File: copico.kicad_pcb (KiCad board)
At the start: 2 copper layers, 100 x 96 mm, 33 parts, among them P1 CocoEdgeConnector, P10 Power Bus, P2 5V Data Bus, P3 3.3V Data Bus, P4 5V Address Bus, P5 3.3V Address Bus, U1 74LS133, U2 74LS06, U3 PicoW, U4 TRANSCEIVER-8BIT, U5 TRANSCEIVER-8BIT, U6 TRANSCEIVER-8BIT, U7 SN74LVC4245A, U8 TRANSCEIVER-8BIT

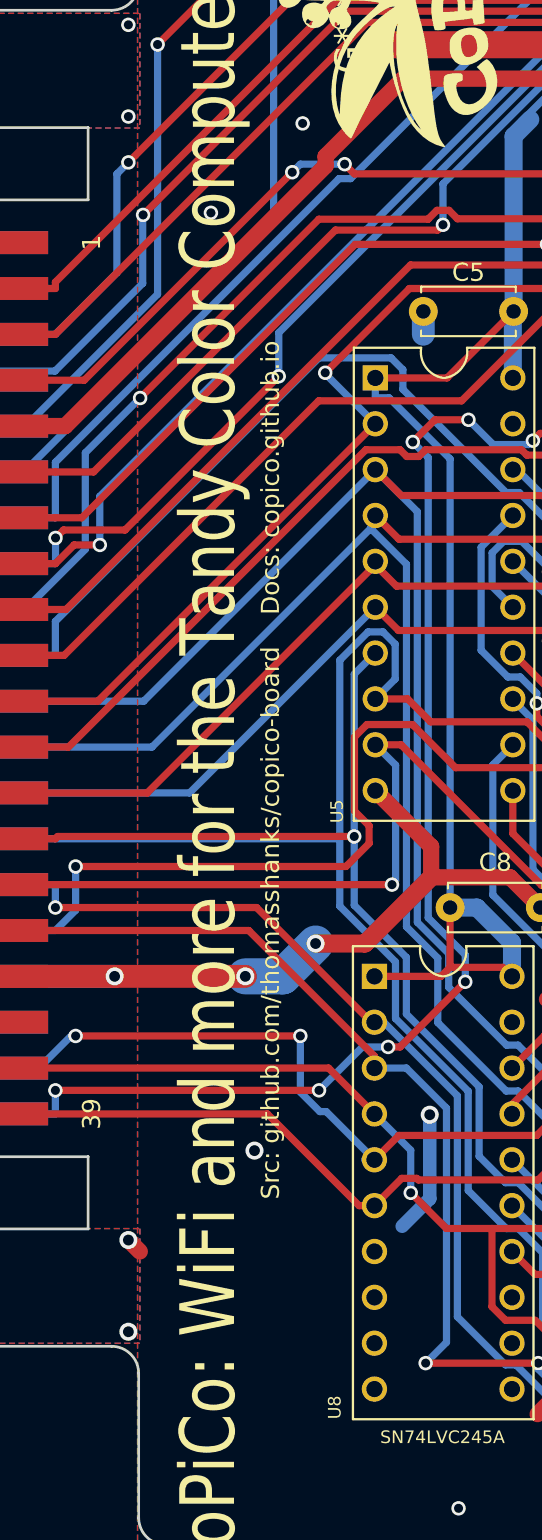
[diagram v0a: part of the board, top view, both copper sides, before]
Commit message: Correct signal naming on schematic & URL on PCB
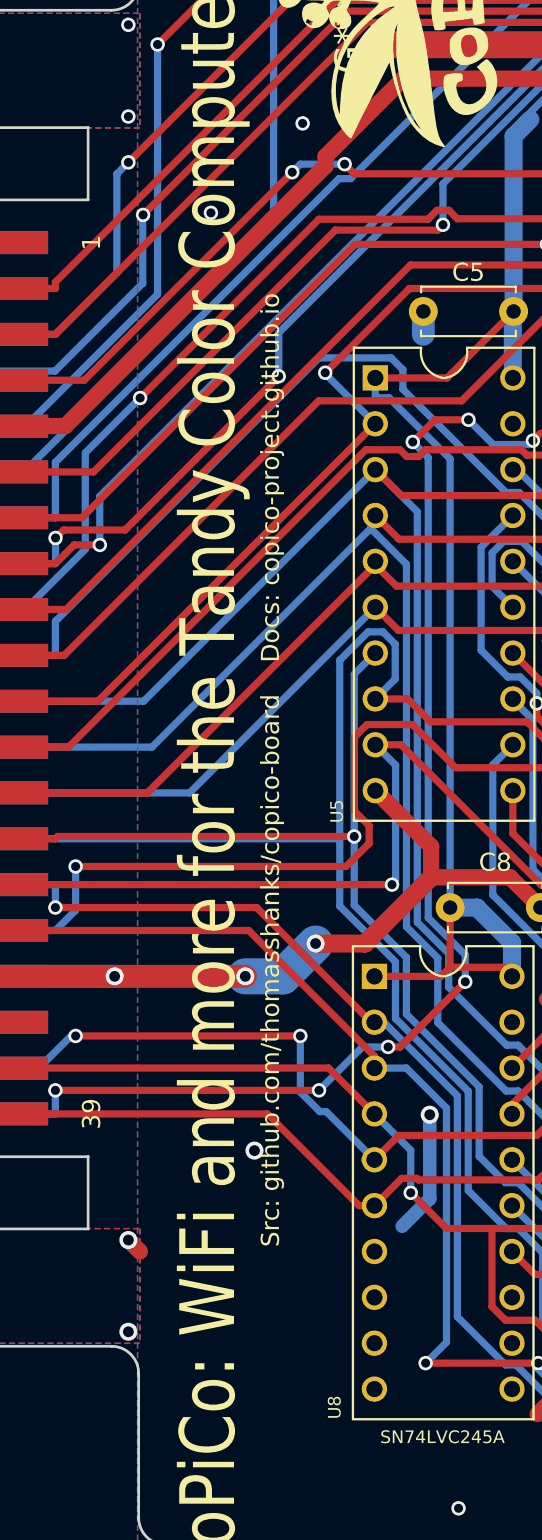
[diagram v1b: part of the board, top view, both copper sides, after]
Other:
- board text added: "Src: github.com/thomasshanks/copico-board Docs: copico-project.github.io"
- board text removed: "Src: github.com/thomasshanks/copico-board Docs: copico.github.io"
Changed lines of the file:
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@@
   (title_block
     (title "CoPiCo: WiFi and more for the Tandy Color Computer")
-    (date "2024-02-07")
-    (rev "0.2.1")
+    (date "2024-02-18")
+    (rev "0.1.22")
     (company "Thomas Shanks (copico@tshanks.org)")
-    (comment 1 "https://github.com/JayesonLS/TandyCircuitsAndLogic/tree/master/CoCoProtoBoard")
-    (comment 2 "Board footprint based on the Public Domain CoCoProtoBoard:")
-    (comment 4 "https://github.com/thomasshanks/copico-board")
+    (comment 1 "found at: github.com/JayesonLS/TandyCircuitsAndLogic/tree/master/CoCoProtoBoard")
+    (comment 2 "Board footprint based on the Public Domain CoCoProtoBoard, which can be")
+    (comment 3 "Released under the MIT License (opensource.org/license/mit)")
+    (comment 4 "GitHub Repo: https://github.com/thomasshanks/copico-board")
   )
   (layers
@@
     (effects (font (size 1.0668 1.0668) (thickness 0.1778)) (justify left bottom mirror))
   )
-  (gr_text "Src: github.com/thomasshanks/copico-board    Docs: copico.github.io" (at 110.744 109.22 90) (layer "F.SilkS")
+  (gr_text "Src: github.com/thomasshanks/copico-board    Docs: copico-project.github.io" (at 110.744 109.22 90) (layer "F.SilkS")
     (effects (font (size 1 1) (thickness 0.15)))
   )

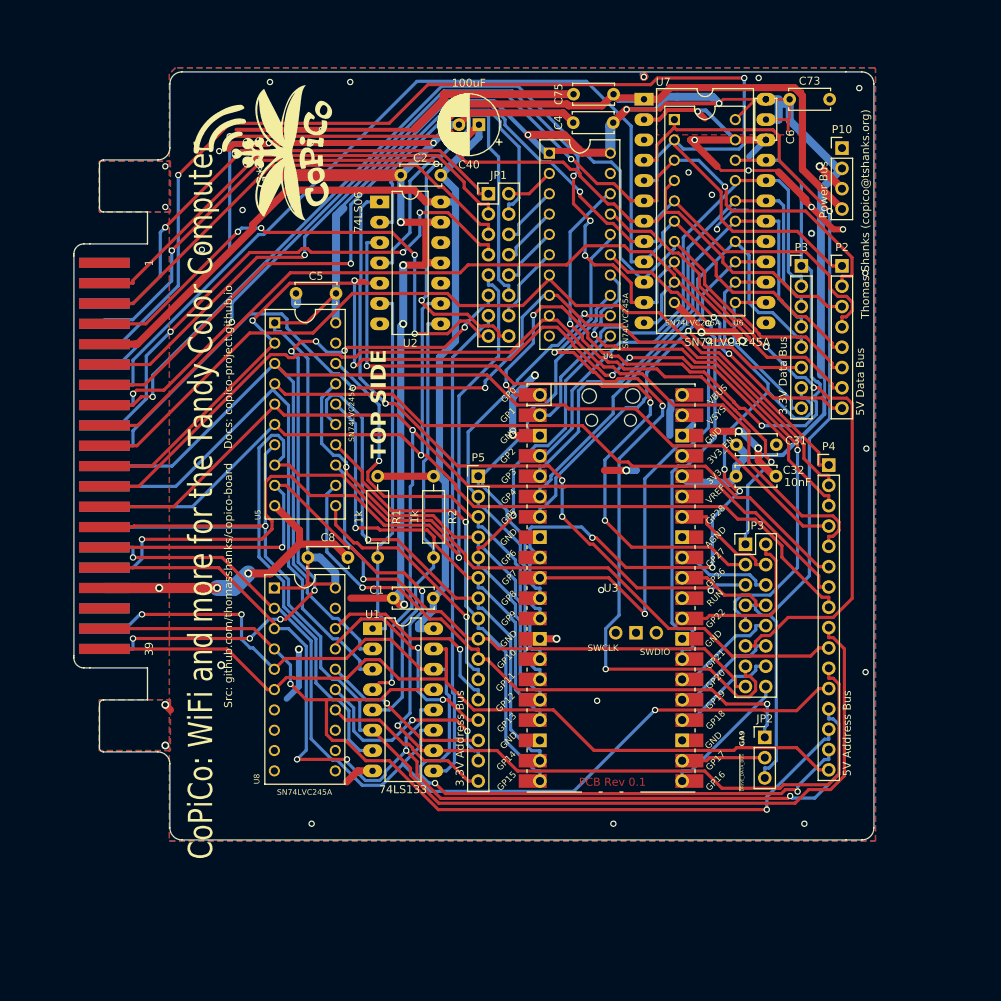
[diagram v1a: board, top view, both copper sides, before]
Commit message: Update silkscreen with component values
I accidentally left the component value silkscreening off the first run of the
board. Add these back, as well as adding some labels to the jumpers and such.

Update PCB Rev in solder mask to 0.1a, but leave the copper layer PCB Rev at
0.1 since that layer has not changed.
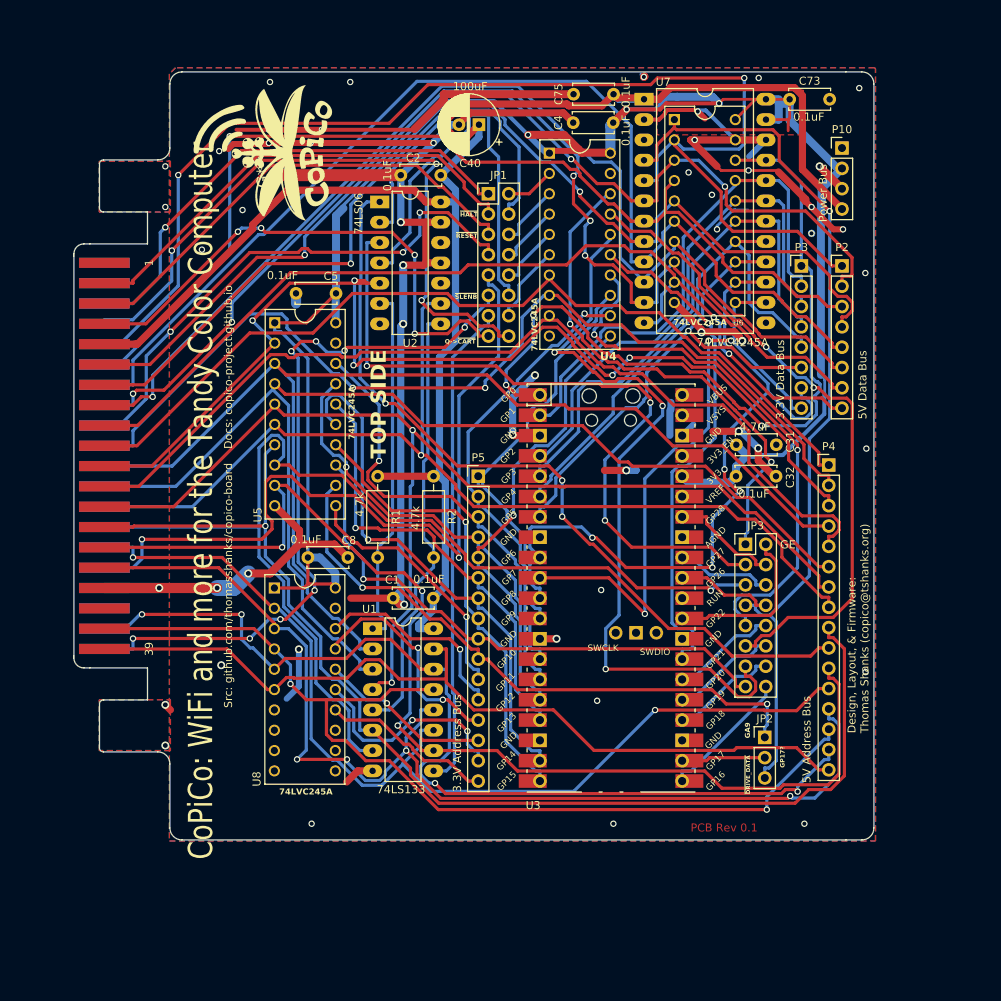
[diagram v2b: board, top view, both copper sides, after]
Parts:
- removed C6: 1uF, 00_Custom:C_Disc_D5.0mm_W2.5mm_P200mils
- C1, C2, C4, C5, C73, C75, C8: value 1uF -> 0.1uF
- C31: value 1uF -> 4.7uF
- C32: value 10nF -> 0.1uF
- R1, R2: value 1k -> 4.7k
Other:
- board text added: "0.1uF"
- board text added: "100uF"
- board text added: "3.3V Address Bus"
- board text added: "3.3V Data Bus"
- board text added: "4.7k"
- board text added: "4.7uF"
- board text added: "5V Address Bus"
- board text added: "5V Data Bus"
- board text added: "74LS06"
- board text added: "74LS133"
- board text added: "74LVC245A"
- board text added: "74LVC4245A"
- board text added: "Design, Layout, & Firmware: Thomas Shanks (copico@tshanks.org)"
- board text added: "GE"
- board text added: "GP17?"
- board text added: "PCB Rev 0.1a"
- board text added: "Power Bus"
- board text added: "Q->~{CART}"
- board text added: "~{DRIVE_DATA}"
- board text added: "~{HALT}"
- board text added: "~{RESET}"
- board text added: "~{SLENB}"
- board text removed: "Thomas Shanks (copico@tshanks.org)"
- board text removed: "~{DRIVE_DATA_BUS}"

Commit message: Update PCB layout with Rev 0.2 schematic changes
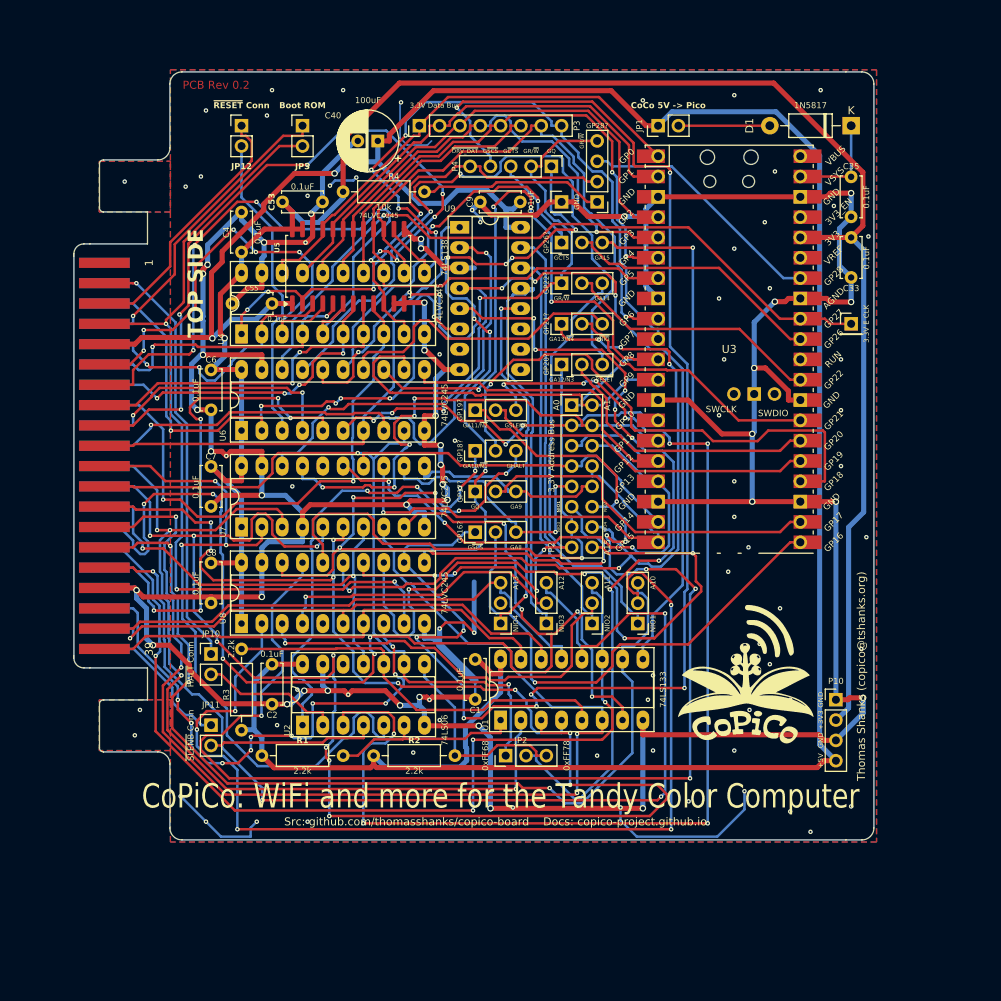
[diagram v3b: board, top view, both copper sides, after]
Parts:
- removed C31: 4.7uF, Capacitor_THT:C_Disc_D5.0mm_W2.5mm_P5.00mm
- removed C32, C5, C73, C75: 0.1uF, Capacitor_THT:C_Disc_D5.0mm_W2.5mm_P5.00mm
- removed the G*** at (185.7, 149.4)
- removed P5: 3.3V Address Bus, Connector_PinHeader_2.54mm:PinHeader_1x16_P2.54mm_Vertical
- added C33: 0.1uF, Capacitor_THT:C_Disc_D5.0mm_W2.5mm_P5.00mm, F.Cu at (188.6, 76.8)
- added C35: 0.1uF, Capacitor_THT:C_Disc_D5.0mm_W2.5mm_P5.00mm, F.Cu at (188.6, 69.3)
- added C53: 0.1uF, Capacitor_THT:C_Disc_D5.0mm_W2.5mm_P5.00mm, F.Cu at (117.5, 72.4)
- added C55: 0.1uF, Capacitor_THT:C_Disc_D5.0mm_W2.5mm_P5.00mm, F.Cu at (116.2, 85.1)
- added C6: 0.1uF, Capacitor_THT:C_Disc_D5.0mm_W2.5mm_P5.00mm, F.Cu at (108.6, 93.4)
- added C7: 0.1uF, Capacitor_THT:C_Disc_D5.0mm_W2.5mm_P5.00mm, F.Cu at (108.6, 105.5)
- added C9: 0.1uF, Capacitor_THT:C_Disc_D5.0mm_W2.5mm_P5.00mm, F.Cu at (147.2, 72.4)
- added D1: 1N5817, Diode_THT:D_DO-41_SOD81_P10.16mm_Horizontal, F.Cu at (188.6, 62.9)
- added G0: LOGO, 00_Custom:logo_small, F.Cu at (188.0, 149.2)
- added JP10: Jumper_2_Open, Connector_PinHeader_2.54mm:PinHeader_1x02_P2.54mm_Vertical, F.Cu at (108.6, 128.9)
- added JP101: J3_C12, Connector_PinHeader_2.54mm:PinHeader_1x03_P2.54mm_Vertical, F.Cu at (141.6, 113.7)
- added JP102: J3_C12, Connector_PinHeader_2.54mm:PinHeader_1x03_P2.54mm_Vertical, F.Cu at (141.6, 108.6)
- added JP103: J3_C12, Connector_PinHeader_2.54mm:PinHeader_1x03_P2.54mm_Vertical, F.Cu at (161.9, 125.1)
- added JP104: J3_C12, Connector_PinHeader_2.54mm:PinHeader_1x03_P2.54mm_Vertical, F.Cu at (156.2, 125.1)
- added JP105: J3_C12, Connector_PinHeader_2.54mm:PinHeader_1x03_P2.54mm_Vertical, F.Cu at (141.6, 103.5)
- added JP106: J3_C12, Connector_PinHeader_2.54mm:PinHeader_1x03_P2.54mm_Vertical, F.Cu at (141.6, 98.4)
- added JP107: J3_C12, Connector_PinHeader_2.54mm:PinHeader_1x03_P2.54mm_Vertical, F.Cu at (150.5, 125.1)
- added JP108: J3_C12, Connector_PinHeader_2.54mm:PinHeader_1x03_P2.54mm_Vertical, F.Cu at (144.8, 125.1)
- added JP109: J3_C12, Connector_PinHeader_2.54mm:PinHeader_1x03_P2.54mm_Vertical, F.Cu at (152.4, 92.7)
- added JP11: Jumper_2_Open, Connector_PinHeader_2.54mm:PinHeader_1x02_P2.54mm_Vertical, F.Cu at (108.6, 137.8)
- added JP110: J3_C12, Connector_PinHeader_2.54mm:PinHeader_1x03_P2.54mm_Vertical, F.Cu at (152.4, 87.6)
- added JP111: J3_C12, Connector_PinHeader_2.54mm:PinHeader_1x03_P2.54mm_Vertical, F.Cu at (152.4, 82.5)
- added JP112: J3_C12, Connector_PinHeader_2.54mm:PinHeader_1x03_P2.54mm_Vertical, F.Cu at (152.4, 77.5)
- added JP12: Jumper_2_Bridged, Connector_PinHeader_2.54mm:PinHeader_1x02_P2.54mm_Vertical, F.Cu at (112.4, 62.9)
- added JP4: jp_ser_4pin_23cl, Connector_PinHeader_2.54mm:PinHeader_1x04_P2.54mm_Vertical, F.Cu at (156.8, 72.4)
- added R3: 2.2K, Resistor_THT:R_Axial_DIN0207_L6.3mm_D2.5mm_P10.16mm_Horizontal, F.Cu at (112.4, 138.4)
- added R4: 10k, Resistor_THT:R_Axial_DIN0207_L6.3mm_D2.5mm_P10.16mm_Horizontal, F.Cu at (125.1, 71.1)
- added TP1: TestPoint, Connector_PinHeader_2.54mm:PinHeader_1x01_P2.54mm_Vertical, F.Cu at (152.4, 72.4)
- added TP2: TestPoint, Connector_PinHeader_2.54mm:PinHeader_1x01_P2.54mm_Vertical, F.Cu at (188.6, 87.6)
- added U9: 74LS138, Package_DIP:DIP-16_W7.62mm_Socket_LongPads, F.Cu at (139.7, 75.6)
- JP1, JP3: value 8JP2NC -> Jumper_2_Open; footprint Connector_PinHeader_2.54mm:PinHeader_2x08_P2.54mm_Vertical -> Connector_PinHeader_2.54mm:PinHeader_1x02_P2.54mm_Vertical
- P2: value 5V Data Bus -> 3.3V Address Bus; footprint Connector_PinHeader_2.54mm:PinHeader_1x08_P2.54mm_Vertical -> Connector_PinHeader_2.54mm:PinHeader_2x08_P2.54mm_Vertical
- P4: value 5V Address Bus -> Debug; footprint Connector_PinHeader_2.54mm:PinHeader_1x16_P2.54mm_Vertical -> Connector_PinHeader_2.54mm:PinHeader_1x05_P2.54mm_Vertical
- R1, R2: value 4.7k -> 2.2K
- U1: footprint Package_DIP:DIP-16_W7.62mm_LongPads -> Package_DIP:DIP-16_W7.62mm_Socket_LongPads
- U2: footprint Package_DIP:DIP-14_W7.62mm_LongPads -> Package_DIP:DIP-14_W7.62mm_Socket_LongPads
- U4, U6, U8: footprint LOGIC-SN74LVC245AN_DIP20-7.62MM_:DIP20-2.54-26.2X7.62MM -> Package_DIP:DIP-20_W7.62mm_Socket_LongPads
- U5: value TRANSCEIVER-8BIT -> SN74LVC4245A; footprint LOGIC-SN74LVC245AN_DIP20-7.62MM_:DIP20-2.54-26.2X7.62MM -> Package_SO:SOIC-24W_7.5x15.4mm_P1.27mm
- U7: value SN74LVC4245A -> TRANSCEIVER-8BIT; footprint 00_Custom:MDFLY_MOL-CV0089_SN74LVC4245A -> Package_DIP:DIP-20_W7.62mm_Socket_LongPads
- moved G2 85.9 mm to (173.4, 131.4), turned to 0 degrees
- moved JP3 76.2 mm to (120.0, 62.9)
- moved U7 73.4 mm to (112.4, 113.0), turned to 90 degrees
- moved P10 69.0 mm to (186.7, 134.6)
- moved U2 66.1 mm to (120.0, 137.8), turned to 90 degrees
- moved C2 64.7 mm to (116.2, 130.2), turned to -90 degrees
- moved U6 64.1 mm to (112.4, 101.0), turned to 90 degrees
- moved P4 51.0 mm to (151.1, 67.9), turned to -90 degrees
- moved P3 50.9 mm to (134.6, 62.9), turned to 90 degrees
- moved C4 47.8 mm to (112.4, 73.7), turned to -90 degrees
- moved U4 43.7 mm to (112.4, 88.9), turned to 90 degrees
- moved P2 38.0 mm to (153.7, 97.8)
- moved R1 37.8 mm to (114.9, 141.6), turned to 0 degrees
- moved R2 35.7 mm to (128.9, 141.6), turned to 0 degrees
- moved U3 33.3 mm to (173.4, 90.8)
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- renumbered G*** to G2
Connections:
- C4 pad 1: +3V3 -> GND
- C4 pad 2: GND -> +3V3
- JP1 pad 1: Net-(JP1A-A) -> +5V
- JP1 pad 2: /E -> Net-(D1-A)
- JP2 pad 1: /GA9 -> /A4
- JP2 pad 2: /GA9_OR_~{DRIVE_DATA_BUS} -> Net-(JP2-C)
- JP2 pad 3: /~{DRIVE_DATA_BUS} -> /~{A4}
- JP3 pad 1: /GE -> /~{CART}
- JP3 pad 2: Net-(JP3A-B) -> /Q
- P1 pad 18: Net-(JP1D-A) -> /R/~{W}
- P1 pad 3: Net-(JP1B-A) -> Net-(JP10-A)
- P1 pad 32: Net-(JP1E-A) -> /~{CTS}
- P1 pad 36: unconnected-(P1-~{SCS}-Pad36) -> /~{SCS}
- P1 pad 40: Net-(JP1F-A) -> Net-(JP11-A)
- P1 pad 5: Net-(JP1C-A) -> Net-(JP12-A)
- P1 pad 6: Net-(JP1A-A) -> /E
- P1 pad 7: Net-(JP1H-A) -> /Q
- P1 pad 8: Net-(JP1H-B) -> /~{CART}
- P2 pad 1: /D0 -> /GA0
- P2 pad 2: /D1 -> /GA1
- P2 pad 3: /D2 -> /GA2
- P2 pad 4: /D3 -> /GA3
- P2 pad 5: /D4 -> /GA4
- P2 pad 6: /D5 -> /GA5
- P2 pad 7: /D6 -> /GA6
- P2 pad 8: /D7 -> /GA7
- P4 pad 1: /A0 -> /GQ
- P4 pad 2: /A1 -> /GR/~{W}
- P4 pad 3: /A2 -> /G~{CTS}
- P4 pad 4: /A3 -> /G~{SCS}
- P4 pad 5: /A4 -> /~{DRIVE_DATA_BUS}
- R2 pad 2: /~{A7} -> /~{A4}
- U1 pad 9: Net-(JP1G-A) -> /~{NETIO_SEL}
- U2 pad 1: /G~{HALT} -> /GHALT
- U2 pad 10: unconnected-(U2-Pad10) -> /~{A7}
- U2 pad 11: GND -> /A7
- U2 pad 3: /G~{SLENB} -> /GSLENB
- U2 pad 8: /~{A7} -> /~{A4}
- U2 pad 9: /A7 -> /A4
- U3 pad 21: Net-(JP3H-B) -> /GA8_OR_G~{SCS}
- U3 pad 22: /GA9_OR_~{DRIVE_DATA_BUS} -> /GA9_OR_GQ
- U3 pad 24: Net-(JP3G-B) -> /GPIO18
- U3 pad 25: Net-(JP3F-B) -> /GPIO19
- U3 pad 26: Net-(JP3E-B) -> /GPIO20
- U3 pad 27: /G~{CTS} -> /GPIO21
- U3 pad 29: Net-(JP3A-B) -> /GA14_OR_GR/~{W}
- U3 pad 31: Net-(JP3D-B) -> /GA15_OR_G~{CTS}
- U3 pad 32: Net-(JP3C-B) -> /GE
- U3 pad 33: unconnected-(U3-AGND-Pad33) -> GND
- U3 pad 34: Net-(JP3B-B) -> /~{DRIVE_DATA_BUS}_OR_GR/~{W}
- U3 pad 39: unconnected-(U3-VSYS-Pad39) -> Net-(D1-K)
- U4 pad 1: +3V3 -> /~{DRIVE_DATA_BUS}
- U4 pad 11: /GA4 -> /GD7
- U4 pad 12: /GA1 -> /GD6
- U4 pad 13: /GA0 -> /GD5
- U4 pad 14: /G~{NETIO_SEL} -> /GD4
- U4 pad 15: /G~{CTS} -> /GD3
- U4 pad 16: /GR/~{W} -> /GD2
- U4 pad 17: /G~{RESET} -> /GD1
- U4 pad 18: /GE -> /GD0
- U4 pad 2: /E -> /D0
- U4 pad 3: /~{RESET} -> /D1
- U4 pad 4: /R/~{W} -> /D2
- U4 pad 5: /~{CTS} -> /D3
- U4 pad 6: /~{NETIO_SEL} -> /D4
- U4 pad 7: /A0 -> /D5
- U4 pad 8: /A1 -> /D6
- U4 pad 9: /A4 -> /D7
- U5 pad 1: +3V3 -> +5V
- U5 pad 10: GND -> /D7
- U5 pad 11: /GA10 -> GND
- U5 pad 12: /GA9 -> GND
- U5 pad 13: /GA8 -> GND
- U5 pad 14: /GA7 -> /GD7
- U5 pad 15: /GA6 -> /GD6
- U5 pad 16: /GA5 -> /GD5
- U5 pad 17: /GA3 -> /GD4
- U5 pad 18: /GA2 -> /GD3
- U5 pad 19: GND -> /GD2
- U5 pad 2: /A2 -> /~{DRIVE_DATA_BUS}
- U5 pad 20: +3V3 -> /GD1
- U5 pad 3: /A3 -> /D0
- U5 pad 4: /A5 -> /D1
- U5 pad 5: /A6 -> /D2
- U5 pad 6: /A7 -> /D3
- U5 pad 7: /A8 -> /D4
- U5 pad 8: /A9 -> /D5
- U5 pad 9: /A10 -> /D6
- U6 pad 1: /~{DRIVE_DATA_BUS} -> +3V3
- U6 pad 11: /GD7 -> /GA4
- U6 pad 12: /GD6 -> /GA1
- U6 pad 13: /GD5 -> /GA0
- U6 pad 14: /GD4 -> /G~{NETIO_SEL}
- U6 pad 15: /GD3 -> /G~{CTS}
- U6 pad 16: /GD2 -> /GR/~{W}
- U6 pad 17: /GD1 -> /G~{RESET}
- U6 pad 18: /GD0 -> /GE
- U6 pad 2: /D0 -> /E
- U6 pad 3: /D1 -> /~{RESET}
- U6 pad 4: /D2 -> /R/~{W}
- U6 pad 5: /D3 -> /~{CTS}
- U6 pad 6: /D4 -> /~{NETIO_SEL}
- U6 pad 7: /D5 -> /A0
- U6 pad 8: /D6 -> /A1
- U6 pad 9: /D7 -> /A4
- U7 pad 1: +5V -> +3V3
- U7 pad 10: /D7 -> GND
- U7 pad 11: GND -> /GA9
- U7 pad 12: GND -> /GA8
- U7 pad 13: GND -> /GA7
- U7 pad 14: /GD7 -> /GA6
- U7 pad 15: /GD6 -> /GA5
- U7 pad 16: /GD5 -> unconnected-(U7-B3-Pad16)
- U7 pad 17: /GD4 -> /GA3
- U7 pad 18: /GD3 -> /GA2
- U7 pad 19: /GD2 -> GND
- U7 pad 2: /~{DRIVE_DATA_BUS} -> /A2
- U7 pad 20: /GD1 -> +3V3
- U7 pad 3: /D0 -> /A3
- U7 pad 4: /D1 -> GND
- U7 pad 5: /D2 -> /A5
- U7 pad 6: /D3 -> /A6
- U7 pad 7: /D4 -> /A7
- U7 pad 8: /D5 -> /A8
- U7 pad 9: /D6 -> /A9
- U8 pad 11: unconnected-(U8-B8-Pad11) -> /GQ
- U8 pad 12: unconnected-(U8-B7-Pad12) -> /G~{SCS}
- U8 pad 13: unconnected-(U8-B6-Pad13) -> /GA15
- U8 pad 14: /GA15 -> /GA14
- U8 pad 15: /GA14 -> /GA13_OR_G~{NETIO_SEL4}
- U8 pad 16: /GA13 -> /GA12_OR_G~{NETIO_SEL3}
- U8 pad 17: /GA12 -> /GA11_OR_G~{NETIO_SEL2}
- U8 pad 18: /GA11 -> /GA10_OR_G~{NETIO_SEL1}
- U8 pad 2: /A11 -> /A10_OR_~{NETIO_SEL1}
- U8 pad 3: /A12 -> /A11_OR_~{NETIO_SEL2}
- U8 pad 4: /A13 -> /A12_OR_~{NETIO_SEL3}
- U8 pad 5: /A14 -> unconnected-(U8-A4-Pad5)
- U8 pad 6: /A15 -> /A14
- U8 pad 7: GND -> /A15
- U8 pad 8: GND -> /~{SCS}
- U8 pad 9: GND -> /Q
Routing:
- net GND: track 350.4 -> 623.4 mm, vias 53 -> 109
- net /G~{SCS}: track 0.00 -> 179.8 mm, vias 0 -> 8
- net /GA11_OR_G~{NETIO_SEL2}: track 0.00 -> 171.3 mm, vias 0 -> 7
- net +5V: track 204.7 -> 355.1 mm, vias 0 -> 2
- net /GSLENB: track 0.00 -> 148.4 mm, vias 0 -> 9
- net /A10_OR_~{NETIO_SEL1}: track 0.00 -> 128.3 mm, vias 0 -> 5
- net /D0: track 157.0 -> 35.2 mm
- net /GA15: track 21.6 -> 133.4 mm, vias 0 -> 5
- net /Q: track 0.00 -> 106.4 mm, vias 0 -> 3
- net Net-(JP2-C): track 0.00 -> 100.2 mm, vias 0 -> 7
- net /~{NETIO_SEL}: track 10.0 -> 109.2 mm, vias 0 -> 6
- net /D4: track 139.7 -> 40.8 mm, vias 0 -> 4
- net Net-(JP1E-A): track 97.7 -> 0.00 mm, vias 2 -> 0
- net /GA13_OR_G~{NETIO_SEL4}: track 0.00 -> 97.1 mm, vias 0 -> 5
- net /D5: track 137.4 -> 42.6 mm, vias 1 -> 2
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- removed copper zone on F.Cu, net +3V3
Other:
- rule pad_to_mask_clearance: 0 -> 0.0508
- board text added: "PCB Rev 0.2"
- board text added: "Thanks To: Henry Strickland (strick@yak.net) for the idea, and for adding CoPiCo support to frobio/axiom Phoenix B (GitHub: phoenixvox) for fixing firmware bugs and working with me on the PCB layout Raye Keslensky (raye@lid.cc) for the artwork, and for answering all my KiCad questions"
- board text added: "Thomas Shanks (copico@tshanks.org)"
- board text removed: "0.1uF"
- board text removed: "100uF"
- board text removed: "3.3V Address Bus"
- board text removed: "3.3V Data Bus"
- board text removed: "4.7k"
- board text removed: "4.7uF"
- board text removed: "5V Address Bus"
- board text removed: "5V Data Bus"
- board text removed: "74LS06"
- board text removed: "74LS133"
- board text removed: "74LVC245A"
- board text removed: "74LVC4245A"
- board text removed: "Design, Layout, & Firmware: Thomas Shanks (copico@tshanks.org)"
- board text removed: "GA9"
- board text removed: "GE"
- board text removed: "GP17?"
- board text removed: "PCB Rev 0.1"
- board text removed: "PCB Rev 0.1a"
- board text removed: "Power Bus"
- board text removed: "Q->~{CART}"
- board text removed: "Thanks To: Henry Strickland (strick@yak.net) for the idea, and for adding CoPiCo support to cocoio Raye Keslensky (raye@lid.cc) for the artwork, and for answering all my KiCad questions"
- board text removed: "~{DRIVE_DATA}"
- board text removed: "~{HALT}"
- board text removed: "~{RESET}"
- board text removed: "~{SLENB}"
